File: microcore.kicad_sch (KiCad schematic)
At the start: 5 parts, among them J1 TE_776231-1, J8 USB_B_Mini, M1 Module:mega-mcu100/0.3, M2 Module-power_12and5V-0.3, M3 Module-vr-max9924-0.3

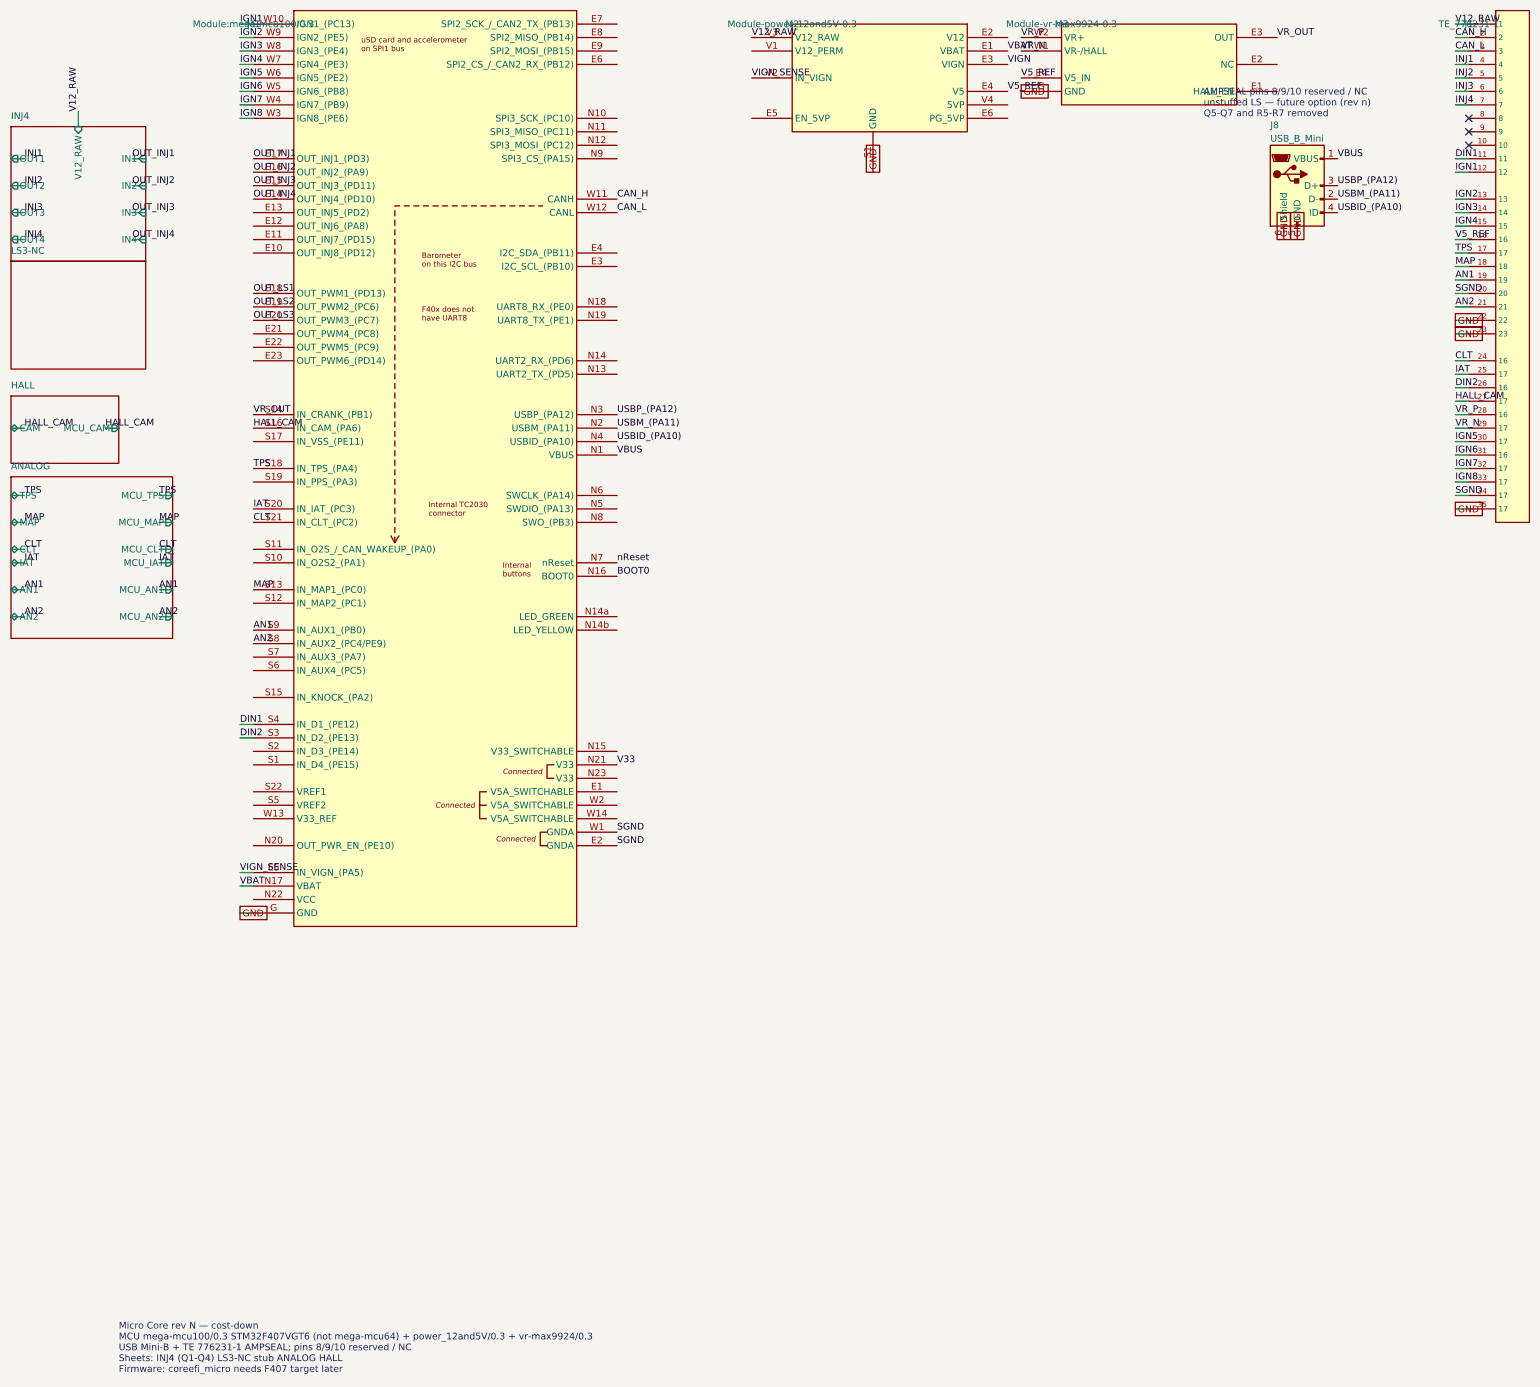
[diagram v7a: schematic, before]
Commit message: Rev o: NCE4080K on Q1-Q7 and restore LS FETs
Swap every power FET from VND14NV04-E to NCE4080K (LCSC C191380,
TO-252-2L) on the existing DPAK land. Bring back Q5-Q7 and gate
R5-R7, and put AMPSEAL pins 8/9/10 back to fuel pump, idle, and boost.

F407VGT6 on mega-mcu100, injector TVS/flyback, Core EFI silk, GND
pours, and the drill origin stay. RDS(on) is rated at 10 V; the
3.3 V gate has no added driver.

Co-authored-by: Quintin <quintinbannink42@users.noreply.github.com>
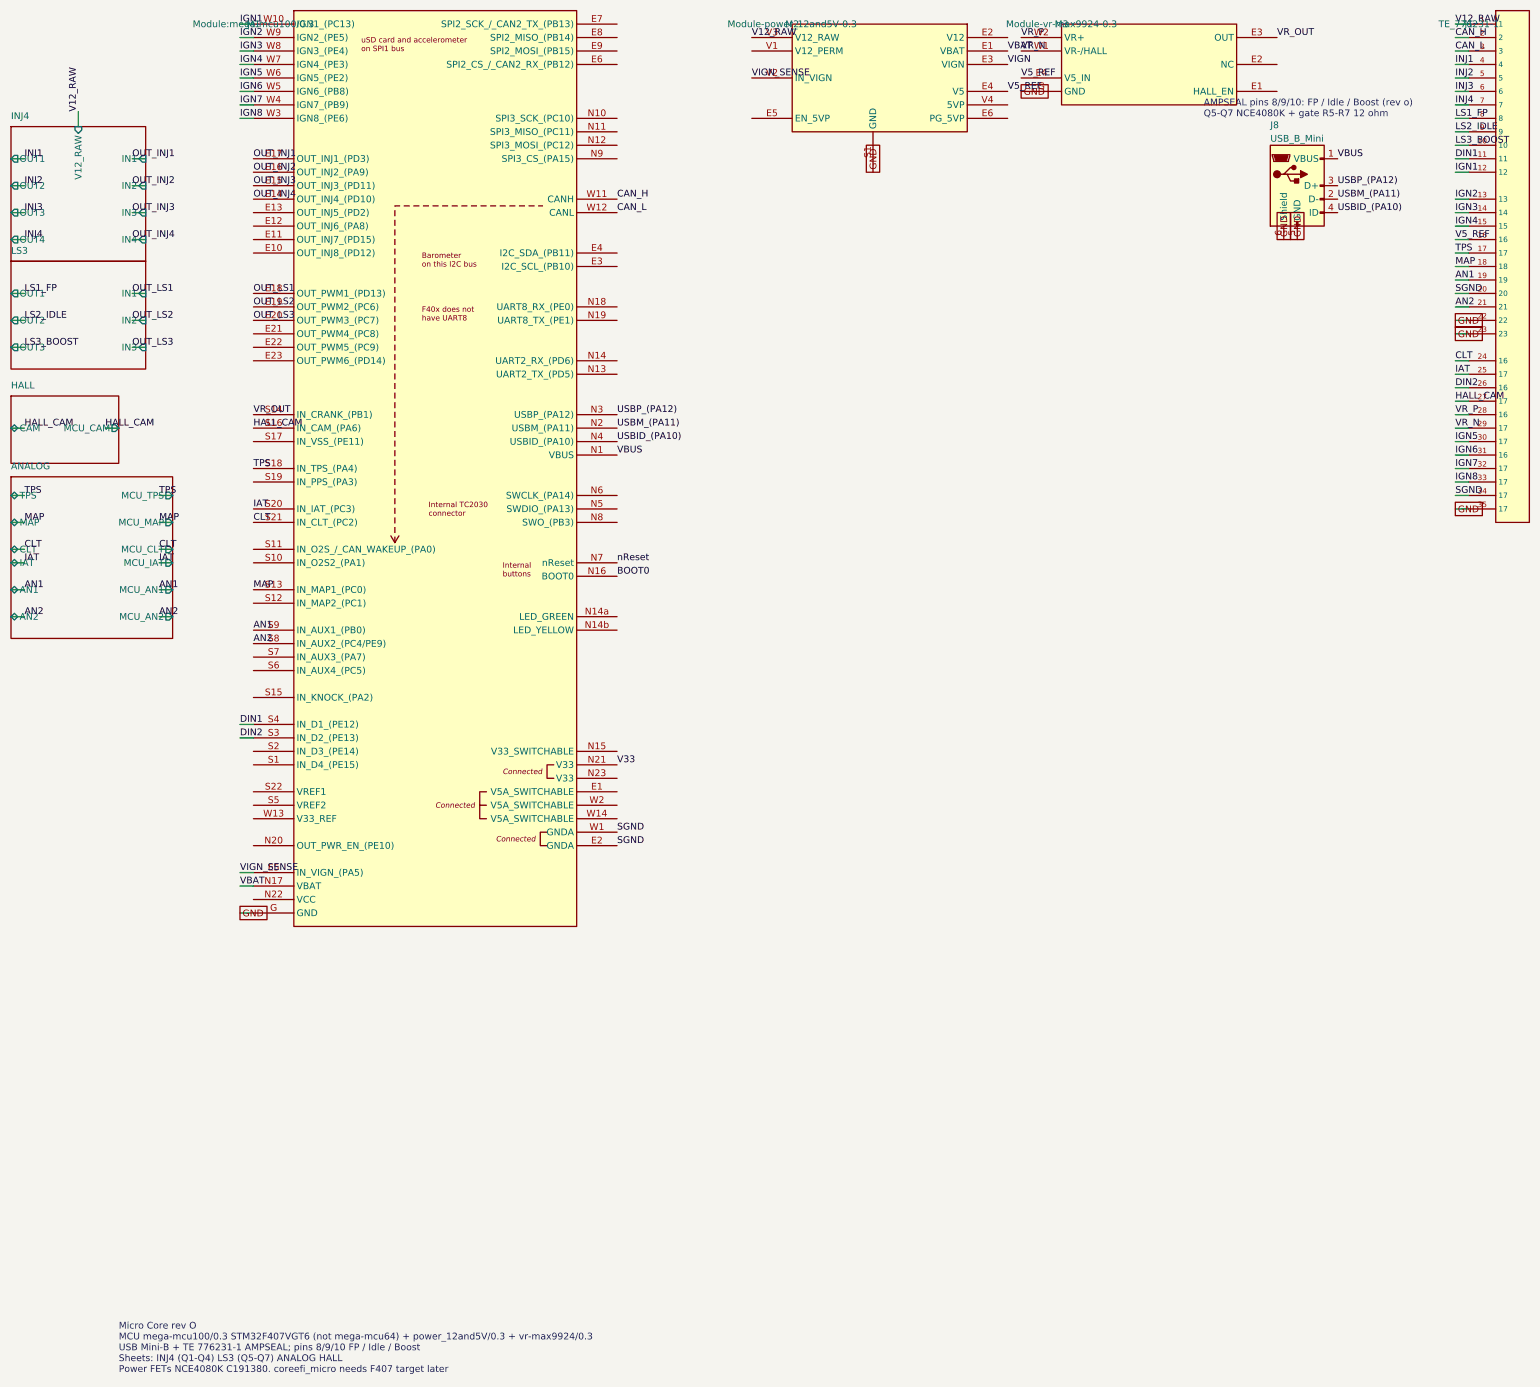
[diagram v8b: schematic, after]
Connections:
- net LS3_BOOST: now reaches J1.10
- net LS1_FP: now reaches J1.8
- net LS2_IDLE: now reaches J1.9
- no-connect marks 3 -> 0
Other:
- sheet LS3-NC renamed LS3
- sheet LS3 ports: added IN1, IN2, IN3, OUT1, OUT2, OUT3; removed none
- note added: "AMPSEAL pins 8/9/10: FP / Idle / Boost (rev o) Q5-Q7 NCE4080K + gate R5-R7 12 ohm"
- note added: "Micro Core rev O MCU mega-mcu100/0.3 STM32F407VGT6 (not mega-mcu64) + power_12and5V/0.3 + vr-max9924/0.3 USB Mini-B + TE 776231-1 AMPSEAL; pins 8/9/10 FP / Idle / Boost Sheets: INJ4 (Q1-Q4) LS3 (Q5-Q7) ANALOG HALL Power FETs NCE4080K C191380. coreefi_micro needs F407 target later"
- note removed: "AMPSEAL pins 8/9/10 reserved / NC unstuffed LS — future option (rev n) Q5-Q7 and R5-R7 removed"
- note removed: "Micro Core rev N — cost-down MCU mega-mcu100/0.3 STM32F407VGT6 (not mega-mcu64) + power_12and5V/0.3 + vr-max9924/0.3 USB Mini-B + TE 776231-1 AMPSEAL; pins 8/9/10 reserved / NC Sheets: INJ4 (Q1-Q4) LS3-NC stub ANALOG HALL Firmware: coreefi_micro needs F407 target later"
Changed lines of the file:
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@@
 		(title "Micro Core")
 		(date "2026-09-22")
-		(rev "N")
+		(rev "O")
 		(company "Core EFI")
-		(comment 1 "rev n cost-down: F407VGT6 on mega-mcu100; LS Q5-Q7 removed")
+		(comment 1 "rev o: NCE4080K Q1-Q7; LS Q5-Q7 restored; F407VGT6 stays")
 		(comment 2 "Firmware board: coreefi_micro — needs F407 target later; fw not in this repo")
 		(comment 3 "PCB basename: microcore (no dashes/underscores)")
@@
 			(color 0 0 0 0.0000)
 		)
-		(property "Sheetname" "LS3-NC"
+		(property "Sheetname" "LS3"
 			(at 5.08 68.87 0)
 			(effects
@@
 				(justify left top)
 				(hide yes)
+			)
+		)
+		(pin "OUT1" output
+			(at 5.08 76.2 180)
+			(effects
+				(font
+					(size 1.27 1.27)
+				)
+				(justify left)
+			)
+		)
+		(pin "OUT2" output
+			(at 5.08 81.28 180)
+			(effects
+				(font
+					(size 1.27 1.27)
+				)
+				(justify left)
+			)
+		)
+		(pin "OUT3" output
+			(at 5.08 86.36 180)
+			(effects
+				(font
+					(size 1.27 1.27)
+				)
+				(justify left)
+			)
+		)
+		(pin "IN1" input
+			(at 30.48 76.2 0)
+			(effects
+				(font
+					(size 1.27 1.27)
+				)
+				(justify right)
+			)
+		)
+		(pin "IN2" input
+			(at 30.48 81.28 0)
+			(effects
+				(font
+					(size 1.27 1.27)
+				)
+				(justify right)
+			)
+		)
+		(pin "IN3" input
+			(at 30.48 86.36 0)
+			(effects
+				(font
+					(size 1.27 1.27)
+				)
+				(justify right)
 			)
 		)
@@
 		)
 	)
-	(text "Micro Core rev N — cost-down\nMCU mega-mcu100/0.3 STM32F407VGT6 (not mega-mcu64) + power_12and5V/0.3 + vr-max9924/0.3\nUSB Mini-B + TE 776231-1 AMPSEAL; pins 8/9/10 reserved / NC\nSheets: INJ4 (Q1-Q4) LS3-NC stub ANALOG HALL\nFirmware: coreefi_micro needs F407 target later"
+	(text "Micro Core rev O\nMCU mega-mcu100/0.3 STM32F407VGT6 (not mega-mcu64) + power_12and5V/0.3 + vr-max9924/0.3\nUSB Mini-B + TE 776231-1 AMPSEAL; pins 8/9/10 FP / Idle / Boost\nSheets: INJ4 (Q1-Q4) LS3 (Q5-Q7) ANALOG HALL\nPower FETs NCE4080K C191380. coreefi_micro needs F407 target later"
 		(exclude_from_sim no)
 		(at 25.4 280 0)
@@
 	(wire
 		(pts
+			(xy 5.08 76.2) (xy 7.62 76.2)
+		)
+		(stroke
+			(width 0)
+			(type default)
+		)
+	)
+	(label "LS1_FP"
+		(at 7.62 76.2 0)
+		(effects
+			(font
+				(size 1.27 1.27)
+			)
+			(justify left bottom)
+		)
+	)
+	(wire
+		(pts
+			(xy 5.08 81.28) (xy 7.62 81.28)
+		)
+		(stroke
+			(width 0)
+			(type default)
+		)
+	)
+	(label "LS2_IDLE"
+		(at 7.62 81.28 0)
+		(effects
+			(font
+				(size 1.27 1.27)
+			)
+			(justify left bottom)
+		)
+	)
+	(wire
+		(pts
+			(xy 5.08 86.36) (xy 7.62 86.36)
+		)
+		(stroke
+			(width 0)
+			(type default)
+		)
+	)
+	(label "LS3_BOOST"
+		(at 7.62 86.36 0)
+		(effects
+			(font
+				(size 1.27 1.27)
+			)
+			(justify left bottom)
+		)
+	)
+	(wire
+		(pts
+			(xy 30.48 76.2) (xy 27.94 76.2)
+		)
+		(stroke
+			(width 0)
+			(type default)
+		)
+	)
+	(label "OUT_LS1"
+		(at 27.94 76.2 180)
+		(effects
+			(font
+				(size 1.27 1.27)
+			)
+			(justify left bottom)
+		)
+	)
+	(wire
+		(pts
+			(xy 30.48 81.28) (xy 27.94 81.28)
+		)
+		(stroke
+			(width 0)
+			(type default)
+		)
+	)
+	(label "OUT_LS2"
+		(at 27.94 81.28 180)
+		(effects
+			(font
+				(size 1.27 1.27)
+			)
+			(justify left bottom)
+		)
+	)
+	(wire
+		(pts
+			(xy 30.48 86.36) (xy 27.94 86.36)
+		)
+		(stroke
+			(width 0)
+			(type default)
+		)
+	)
+	(label "OUT_LS3"
+		(at 27.94 86.36 180)
+		(effects
+			(font
+				(size 1.27 1.27)
+			)
+			(justify left bottom)
+		)
+	)
+	(wire
+		(pts
 			(xy 5.08 114.3) (xy 7.62 114.3)
 		)
@@
 		)
 	)
-	(no_connect
-		(at 280 43.18)
-	)
-	(no_connect
-		(at 280 45.72)
-	)
-	(no_connect
-		(at 280 48.26)
-	)
-	(text "AMPSEAL pins 8/9/10 reserved / NC\nunstuffed LS — future option (rev n)\nQ5-Q7 and R5-R7 removed"
+	(wire
+		(pts
+			(xy 280 43.18) (xy 277.46 43.18)
+		)
+		(stroke
+			(width 0)
+			(type default)
+		)
+	)
+	(label "LS1_FP"
+		(at 277.46 43.18 180)
+		(effects
+			(font
+				(size 1.27 1.27)
+			)
+			(justify left bottom)
+		)
+	)
+	(wire
+		(pts
+			(xy 280 45.72) (xy 277.46 45.72)
+		)
+		(stroke
+			(width 0)
+			(type default)
+		)
+	)
+	(label "LS2_IDLE"
+		(at 277.46 45.72 180)
+		(effects
+			(font
+				(size 1.27 1.27)
+			)
+			(justify left bottom)
+		)
+	)
+	(wire
+		(pts
+			(xy 280 48.26) (xy 277.46 48.26)
+		)
+		(stroke
+			(width 0)
+			(type default)
+		)
+	)
+	(label "LS3_BOOST"
+		(at 277.46 48.26 180)
+		(effects
+			(font
+				(size 1.27 1.27)
+			)
+			(justify left bottom)
+		)
+	)
+	(text "AMPSEAL pins 8/9/10: FP / Idle / Boost (rev o)\nQ5-Q7 NCE4080K + gate R5-R7 12 ohm"
 		(exclude_from_sim no)
 		(at 230 43.18 0)
